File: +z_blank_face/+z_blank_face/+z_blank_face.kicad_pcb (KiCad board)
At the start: 2 copper layers, 85 x 85 mm, 11 parts

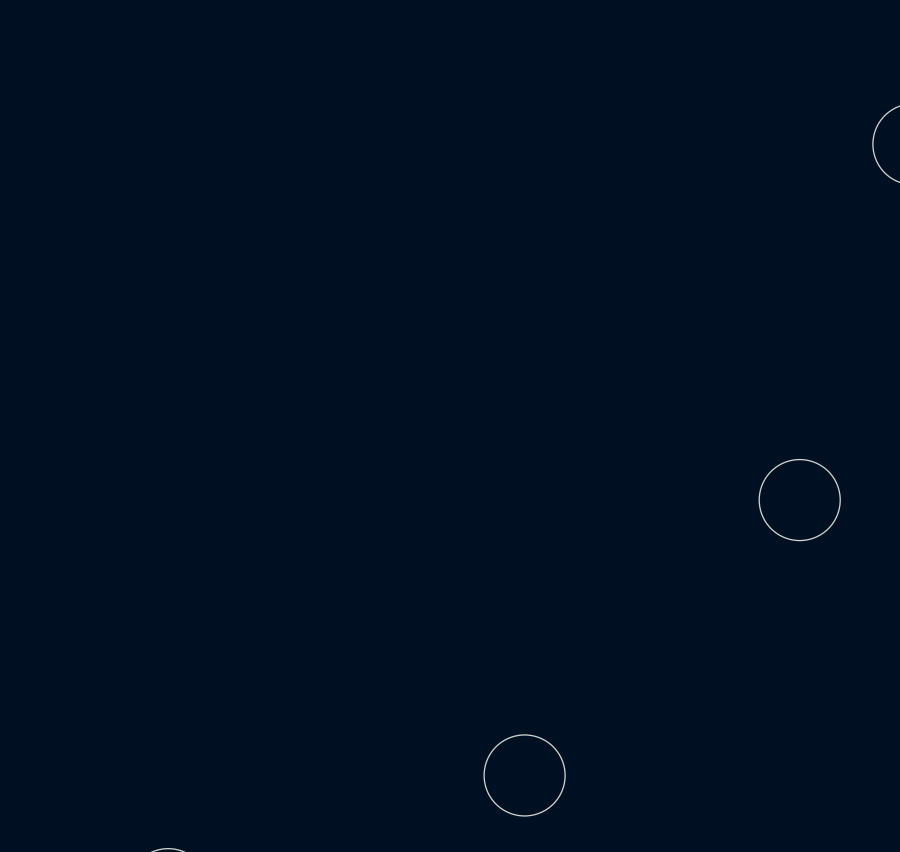
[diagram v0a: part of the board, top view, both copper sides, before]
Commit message: changed cover panels to have smaller power planes, also changed front panel DF13 from SMD to THT
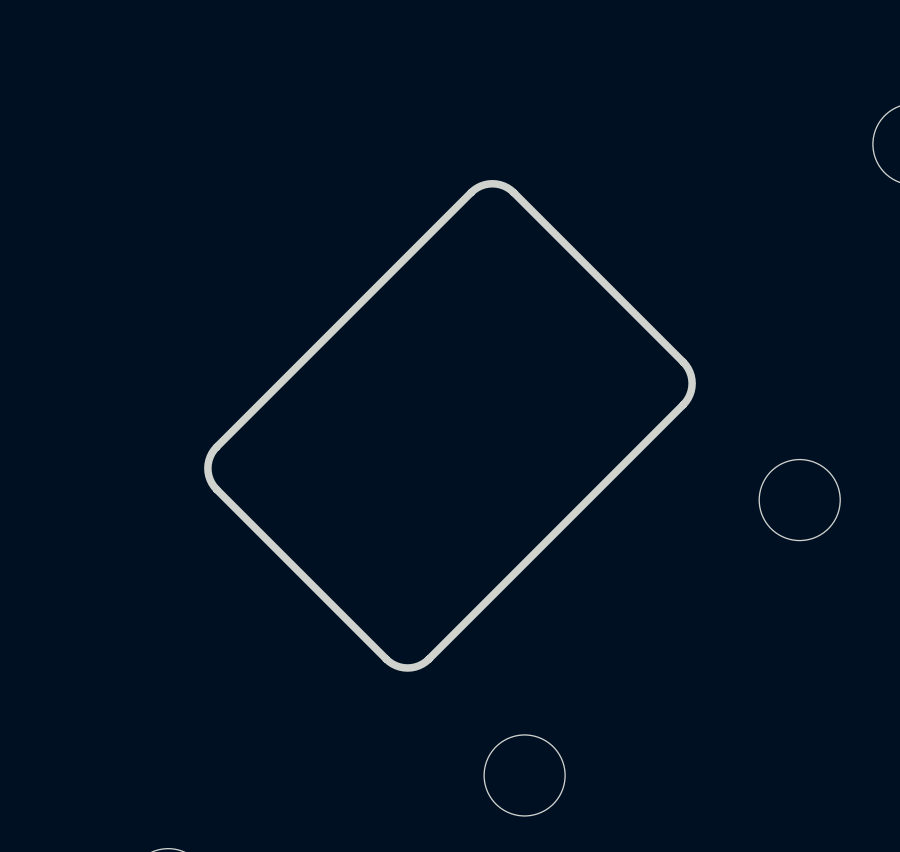
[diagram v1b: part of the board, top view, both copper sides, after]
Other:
- outline, holes or cut-outs redrawn
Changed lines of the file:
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@@
 (kicad_pcb
-	(version 20241229)
+	(version 20260206)
 	(generator "pcbnew")
-	(generator_version "9.0")
+	(generator_version "10.0")
 	(general
 		(thickness 1.6)
@@
 		(pad_to_mask_clearance 0)
 		(allow_soldermask_bridges_in_footprints no)
-		(tenting front back)
+		(tenting
+			(front yes)
+			(back yes)
+		)
+		(covering
+			(front no)
+			(back no)
+		)
+		(plugging
+			(front no)
+			(back no)
+		)
+		(capping no)
+		(filling no)
 		(pcbplotparams
 			(layerselection 0x00000000_00000000_55555555_5755f5ff)
@@
 			(usegerberadvancedattributes yes)
 			(creategerberjobfile yes)
-			(dashed_line_dash_ratio 12.000000)
-			(dashed_line_gap_ratio 3.000000)
+			(dashed_line_dash_ratio 12)
+			(dashed_line_gap_ratio 3)
 			(svgprecision 4)
 			(plotframeref no)
 			(mode 1)
 			(useauxorigin no)
-			(hpglpennumber 1)
-			(hpglpenspeed 20)
-			(hpglpendiameter 15.000000)
 			(pdf_front_fp_property_popups yes)
 			(pdf_back_fp_property_popups yes)
@@
 			(outputformat 1)
 			(mirror no)
-			(drillshape 1)
+			(drillshape 0)
 			(scaleselection 1)
-			(outputdirectory "")
-		)
-	)
-	(net 0 "")
+			(outputdirectory "../../../Board_Order_3/plus_z_cover/")
+		)
+	)
 	(footprint "MountingHole:MountingHole_2.7mm"
 		(layer "F.Cu")
@@
 			(at 0 3.65 0)
 			(layer "F.Fab")
+			(hide yes)
 			(effects
 				(font
@@
 		(sheetfile "+z_blank_face.kicad_sch")
 		(attr exclude_from_pos_files exclude_from_bom)
+		(duplicate_pad_numbers_are_jumpers no)
 		(fp_circle
 			(center 0 0)
@@
 			(at 0 3.65 0)
 			(layer "F.Fab")
+			(hide yes)
 			(effects
 				(font
@@
 		(sheetfile "+z_blank_face.kicad_sch")
 		(attr exclude_from_pos_files exclude_from_bom)
+		(duplicate_pad_numbers_are_jumpers no)
 		(fp_circle
 			(center 0 0)
@@
 			(fill no)
 			(layer "F.CrtYd")
+		)
+		(fp_text user "${REFERENCE}"
+			(at 0 0 0)
+			(layer "F.Fab")
+			(effects
+				(font
+					(size 1 1)
+					(thickness 0.15)
+				)
+			)
 		)
 		(fp_text user "${REFERENCE}"
@@
 			(at 0 3.65 0)
 			(layer "F.Fab")
+			(hide yes)
 			(effects
 				(font
@@
 		(sheetfile "+z_blank_face.kicad_sch")
 		(attr exclude_from_pos_files exclude_from_bom)
+		(duplicate_pad_numbers_are_jumpers no)
 		(fp_circle
 			(center 0 0)
@@
 			(at 0 3.65 0)
 			(layer "F.Fab")
+			(hide yes)
 			(effects
 				(font
@@
 		(sheetfile "+z_blank_face.kicad_sch")
 		(attr exclude_from_pos_files exclude_from_bom)
+		(duplicate_pad_numbers_are_jumpers no)
 		(fp_circle
 			(center 0 0)
@@
 			(fill no)
 			(layer "F.CrtYd")
-		)
-		(fp_text user "${REFERENCE}"
-			(at 0 0 0)
-			(layer "F.Fab")
-			(effects
-				(font
-					(size 1 1)
-					(thickness 0.15)
-				)
-			)
 		)
 		(pad "" np_thru_hole circle
@@
 		(sheetfile "+z_blank_face.kicad_sch")
 		(attr exclude_from_pos_files exclude_from_bom)
+		(duplicate_pad_numbers_are_jumpers no)
 		(fp_circle
 			(center 0 0)
@@
 			(at 0 3.65 0)
 			(layer "F.Fab")
+			(hide yes)
 			(effects
 				(font
@@
 		(sheetfile "+z_blank_face.kicad_sch")
 		(attr exclude_from_pos_files exclude_from_bom)
+		(duplicate_pad_numbers_are_jumpers no)
 		(fp_circle
 			(center 0 0)
@@
 			(at 0 3.65 0)
 			(layer "F.Fab")
+			(hide yes)
 			(effects
 				(font
@@
 		(sheetfile "+z_blank_face.kicad_sch")
 		(attr exclude_from_pos_files exclude_from_bom)
+		(duplicate_pad_numbers_are_jumpers no)
 		(fp_circle
 			(center 0 0)
@@
 			(fill no)
 			(layer "F.CrtYd")
+		)
+		(fp_text user "${REFERENCE}"
+			(at 0 0 0)
+			(layer "F.Fab")
+			(effects
+				(font
+					(size 1 1)
+					(thickness 0.15)
+				)
+			)
 		)
 		(fp_text user "${REFERENCE}"
@@
 			(at 0 3.65 0)
 			(layer "F.Fab")
+			(hide yes)
 			(effects
 				(font
@@
 		(sheetfile "+z_blank_face.kicad_sch")
 		(attr exclude_from_pos_files exclude_from_bom)
+		(duplicate_pad_numbers_are_jumpers no)
 		(fp_circle
 			(center 0 0)
@@
 			(at 0 3.65 0)
 			(layer "F.Fab")
+			(hide yes)
 			(effects
 				(font
@@
 		(sheetfile "+z_blank_face.kicad_sch")
 		(attr exclude_from_pos_files exclude_from_bom)
+		(duplicate_pad_numbers_are_jumpers no)
 		(fp_circle
 			(center 0 0)
@@
 			(fill no)
 			(layer "F.CrtYd")
-		)
-		(fp_text user "${REFERENCE}"
-			(at 0 0 0)
-			(layer "F.Fab")
-			(effects
-				(font
-					(size 1 1)
-					(thickness 0.15)
-				)
-			)
 		)
 		(pad "" np_thru_hole circle
@@
 			(at 0 3.65 0)
 			(layer "F.Fab")
+			(hide yes)
 			(effects
 				(font
@@
 		(sheetfile "+z_blank_face.kicad_sch")
 		(attr exclude_from_pos_files exclude_from_bom)
+		(duplicate_pad_numbers_are_jumpers no)
 		(fp_circle
 			(center 0 0)
@@
 			(fill no)
 			(layer "F.CrtYd")
-		)
-		(fp_text user "${REFERENCE}"
-			(at 0 0 0)
-			(layer "F.Fab")
-			(effects
-				(font
-					(size 1 1)
-					(thickness 0.15)
-				)
-			)
 		)
 		(pad "" np_thru_hole circle
@@
 		(sheetfile "+z_blank_face.kicad_sch")
 		(attr exclude_from_pos_files exclude_from_bom)
+		(duplicate_pad_numbers_are_jumpers no)
 		(fp_circle
 			(center 0 0)
@@
 	)
 	(gr_line
-		(start 185.64 32.86)
-		(end 108.64 32.86)
+		(start 104.64 36.86)
+		(end 104.64 113.86)
 		(stroke
 			(width 0.2)
@@
 	)
 	(gr_arc
+		(start 108.64 117.86)
+		(mid 105.811573 116.688427)
+		(end 104.64 113.86)
+		(stroke
+			(width 0.2)
+			(type default)
+		)
+		(layer "Edge.Cuts")
+	)
+	(gr_line
+		(start 108.64 117.86)
+		(end 185.64 117.86)
+		(stroke
+			(width 0.2)
+			(type default)
+		)
+		(layer "Edge.Cuts")
+	)
+	(gr_arc
+		(start 151.554674 89.678864)
+		(mid 151.261783 88.971758)
+		(end 151.554674 88.26465)
+		(stroke
+			(width 0.25)
+			(type default)
+		)
+		(layer "Edge.Cuts")
+	)
+	(gr_line
+		(start 151.554674 89.678864)
+		(end 157.211528 95.335719)
+		(stroke
+			(width 0.25)
+			(type default)
+		)
+		(layer "Edge.Cuts")
+	)
+	(gr_arc
+		(start 158.625741 95.335719)
+		(mid 157.918635 95.628612)
+		(end 157.211528 95.335719)
+		(stroke
+			(width 0.25)
+			(type default)
+		)
+		(layer "Edge.Cuts")
+	)
+	(gr_line
+		(start 158.625741 95.335719)
+		(end 167.111024 86.850438)
+		(stroke
+			(width 0.25)
+			(type default)
+		)
+		(layer "Edge.Cuts")
+	)
+	(gr_line
+		(start 160.039957 79.77937)
+		(end 151.554674 88.26465)
+		(stroke
+			(width 0.25)
+			(type default)
+		)
+		(layer "Edge.Cuts")
+	)
+	(gr_arc
+		(start 160.039957 79.77937)
+		(mid 160.747064 79.486477)
+		(end 161.45417 79.77937)
+		(stroke
+			(width 0.25)
+			(type default)
+		)
+		(layer "Edge.Cuts")
+	)
+	(gr_line
+		(start 161.45417 79.77937)
+		(end 167.111024 85.436225)
+		(stroke
+			(width 0.25)
+			(type default)
+		)
+		(layer "Edge.Cuts")
+	)
+	(gr_arc
+		(start 167.111024 85.436225)
+		(mid 167.40389 86.143322)
+		(end 167.111024 86.850438)
+		(stroke
+			(width 0.25)
+			(type default)
+		)
+		(layer "Edge.Cuts")
+	)
+	(gr_line
+		(start 185.64 32.86)
+		(end 108.64 32.86)
+		(stroke
+			(width 0.2)
+			(type default)
+		)
+		(layer "Edge.Cuts")
+	)
+	(gr_arc
 		(start 185.64 32.86)
 		(mid 188.468427 34.031573)
-		(end 189.64 36.86)
-		(stroke
-			(width 0.2)
-			(type default)
-		)
-		(layer "Edge.Cuts")
-	)
-	(gr_line
-		(start 104.64 36.86)
-		(end 104.64 113.86)
-		(stroke
-			(width 0.2)
-			(type default)
-		)
-		(layer "Edge.Cuts")
-	)
-	(gr_line
-		(start 189.64 113.86)
 		(end 189.64 36.86)
 		(stroke
@@
 	)
 	(gr_line
-		(start 108.64 117.86)
-		(end 185.64 117.86)
+		(start 189.64 113.86)
+		(end 189.64 36.86)
 		(stroke
 			(width 0.2)
-			(type default)
-		)
-		(layer "Edge.Cuts")
-	)
-	(gr_arc
-		(start 108.64 117.86)
-		(mid 105.811573 116.688427)
-		(end 104.64 113.86)
-		(stroke
-			(width 0.2)
